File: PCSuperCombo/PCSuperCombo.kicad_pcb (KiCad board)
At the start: 2 copper layers, 99.9 x 99.9 mm, 24 parts, among them J1 IDE to CF adapter, J2 CF Adapter Power, J3 Bus_ISA_8bit, SW1 Options, U1 BIOS FLASH, U2 74HCT245, U3 ATF/GAL16V8x-15, U4 DS1315, Y1 32.768 KHz

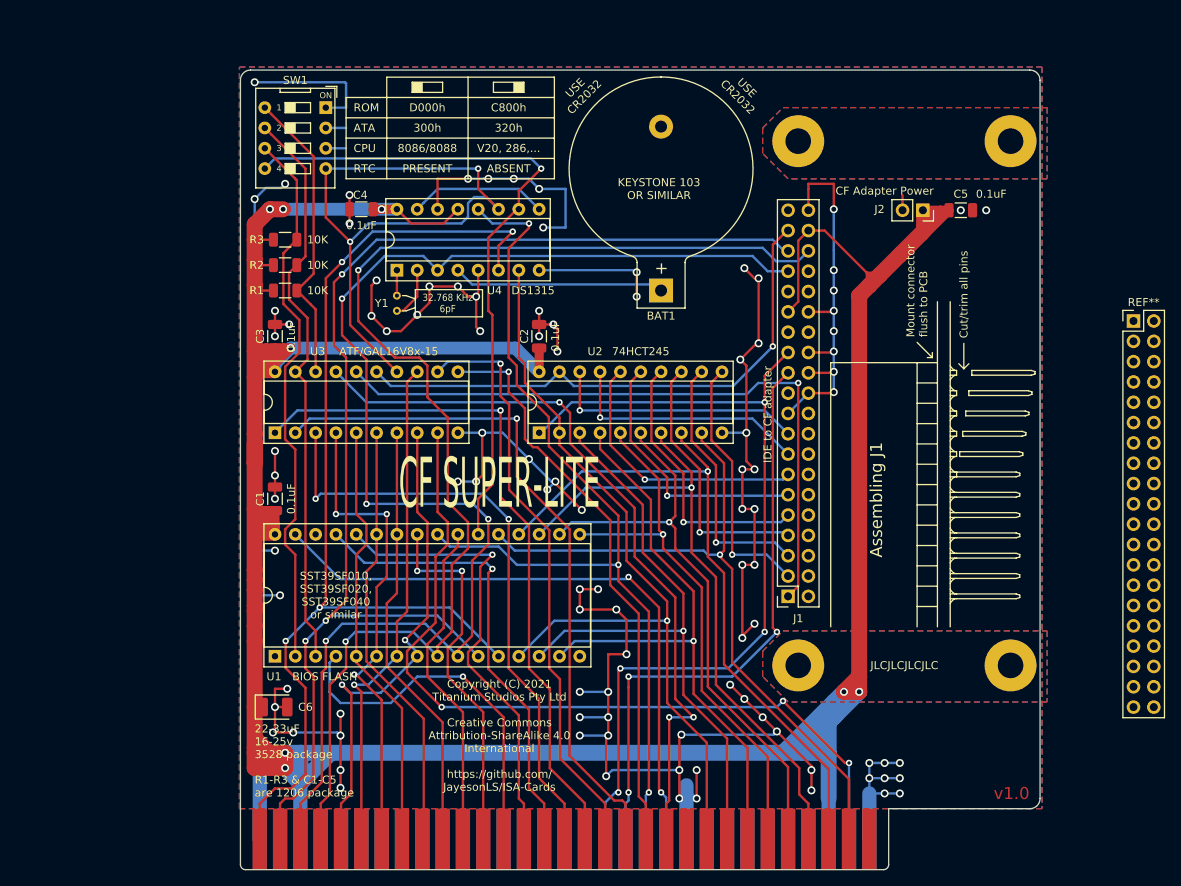
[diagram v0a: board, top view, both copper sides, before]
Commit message: PCSuperCombo: Increase board outline to ~127x107mm.
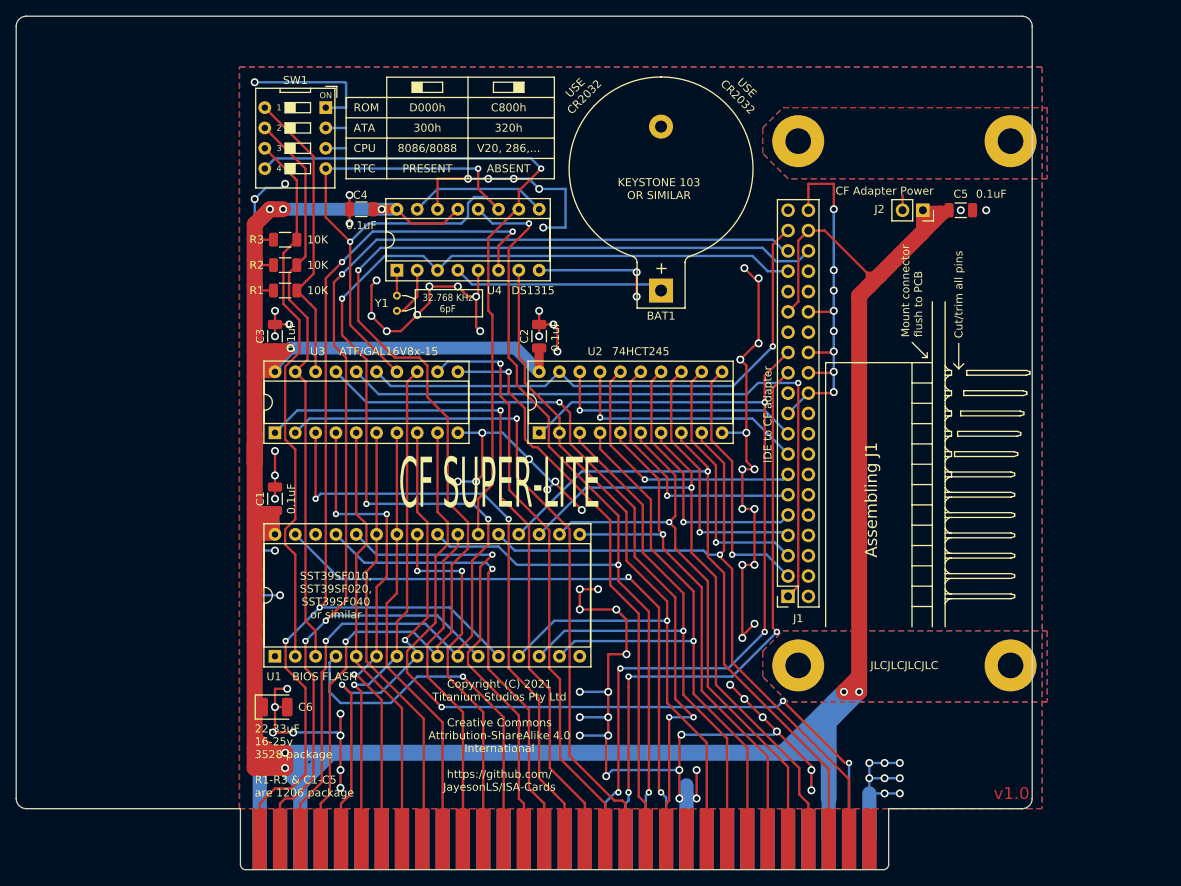
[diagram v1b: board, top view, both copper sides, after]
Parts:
- removed REF**: PinHeader_2x20_P2.54mm_Vertical, Connector_PinHeader_2.54mm:PinHeader_2x20_P2.54mm_Vertical
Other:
- board size 99.9 x 99.9 mm -> 127 x 106.7 mm
- board text added: "Leaves room to take right hand edge to 1mm from back plate. Could be used for a surface mount serial port."
- board text added: "Lowest possible edge - no need to use."
- board text added: "This edge would match top edge of CF adapter"
- board text removed: "The outline is aligned to 0.127mm grid and is sized to fit within the magic 100mm by 100mm size limit set by certain PCB manufaturers for very inexpensive boards."
